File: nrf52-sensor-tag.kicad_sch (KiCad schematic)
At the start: 20 parts, among them IC1 LTR-308ALS-01, IC3 MS860702BA01-50, J3 Conn_01x07_Male, SW1 EVQ-PUA02K, SW2 EVQ-PUA02K, U1 MS88SF2

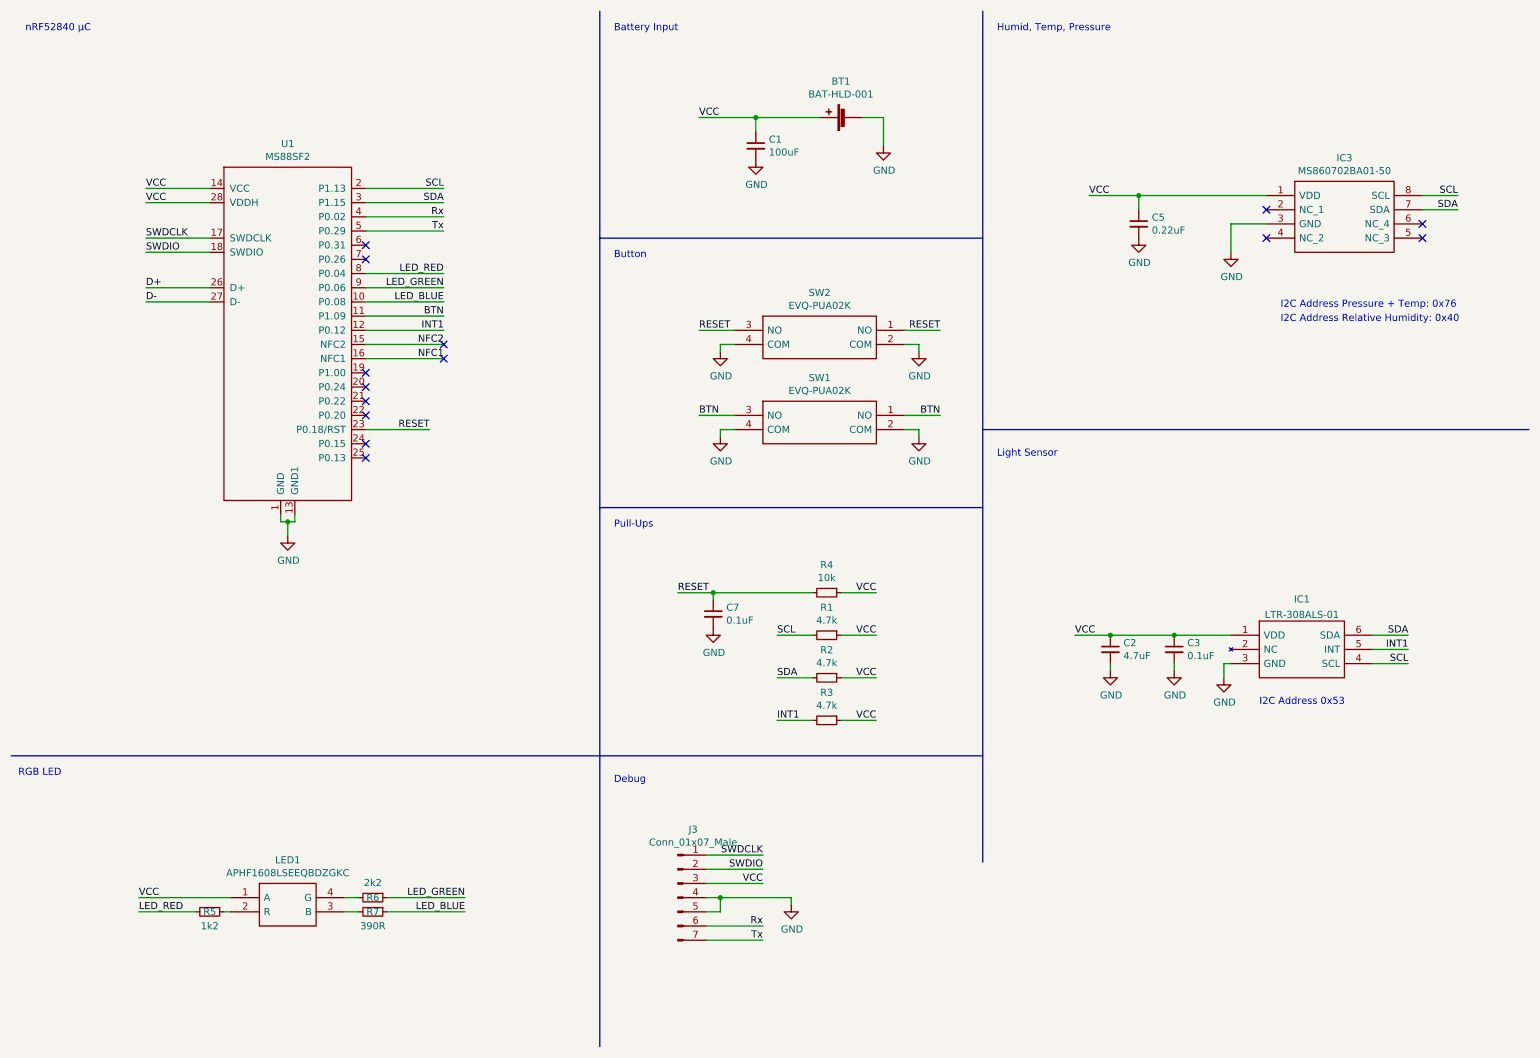
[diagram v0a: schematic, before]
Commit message: Try to fix KiCad Version issue
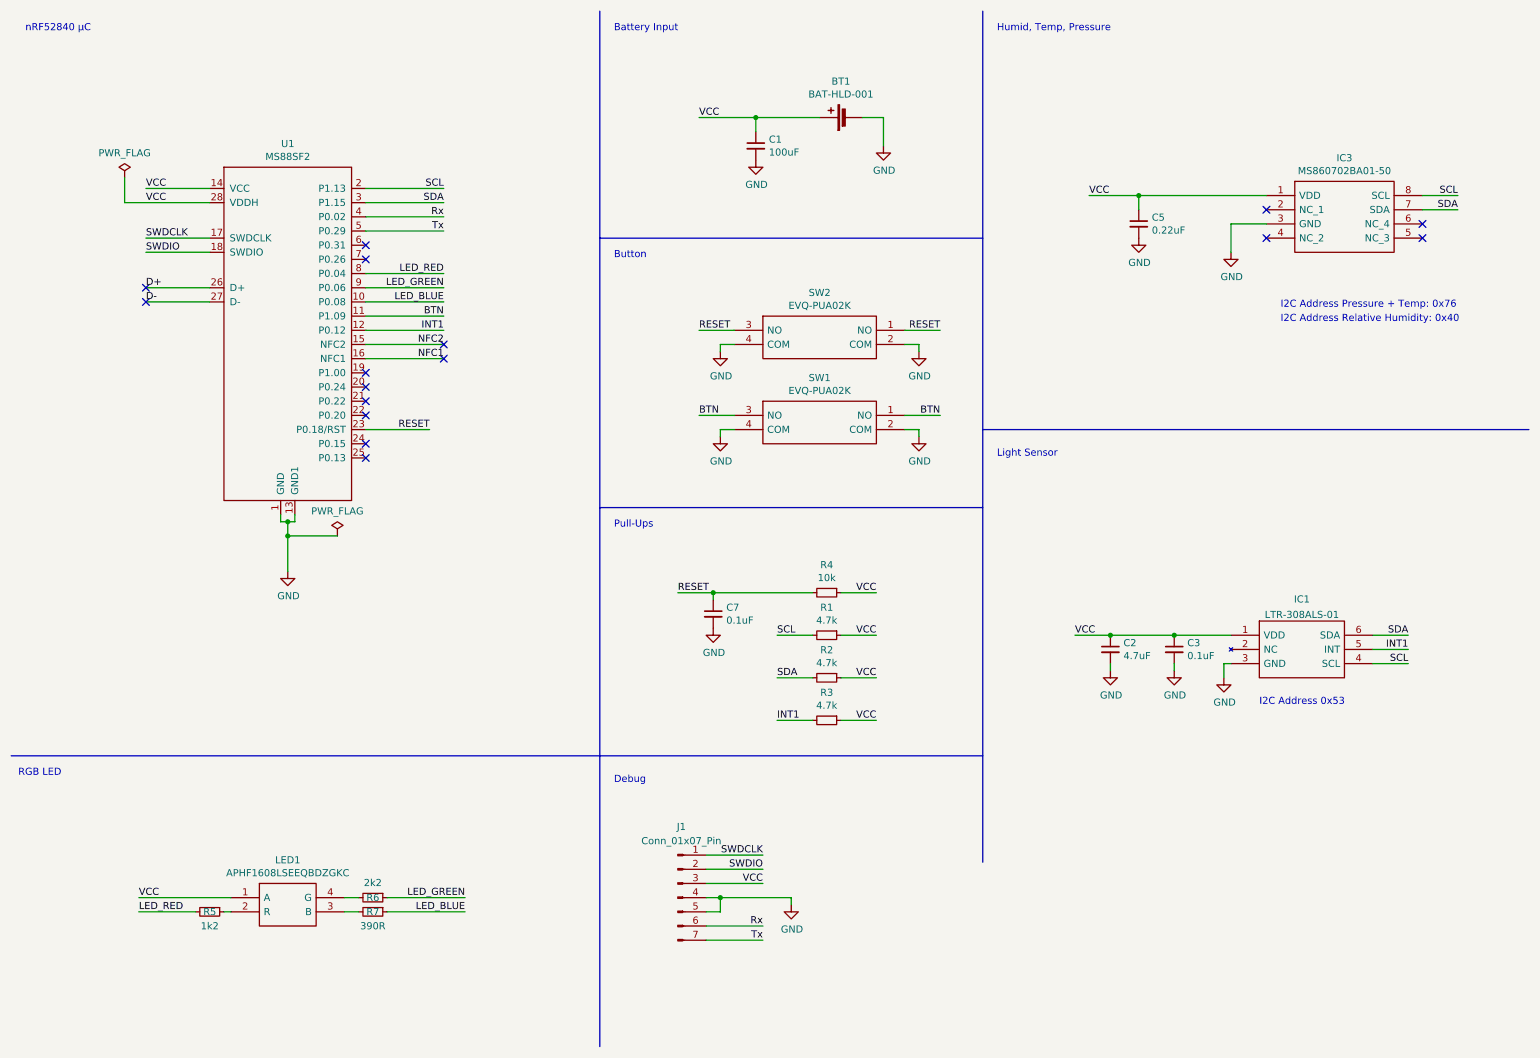
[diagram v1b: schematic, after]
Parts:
- removed J3: Conn_01x07_Male, Connector_PinHeader_2.54mm:PinHeader_1x07_P2.54mm_Vertical, symbol Connector:Conn_01x07_Male
- added J1: Conn_01x07_Pin, Connector_PinSocket_2.54mm:PinSocket_1x07_P2.54mm_Vertical, symbol Connector:Conn_01x07_Pin
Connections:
- net GND: now also J1.4 (Pin_4), J1.5 (Pin_5)
- net Rx: now also J1.6 (Pin_6)
- net SWDCLK: now also J1.1 (Pin_1)
- net SWDIO: now also J1.2 (Pin_2)
- net Tx: now also J1.7 (Pin_7)
- net VCC: now also J1.3 (Pin_3)
- no-connect marks 14 -> 16
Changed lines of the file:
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@@
   (junction (at 139.7 171.45) (diameter 0) (color 0 0 0 0)
   )
+  (junction (at 62.23 104.14) (diameter 0) (color 0 0 0 0)
+  )
   (junction (at 214.63 45.72) (diameter 0) (color 0 0 0 0)
   )
@@
   (junction (at 209.55 124.46) (diameter 0) (color 0 0 0 0)
   )
-  (junction (at 62.23 104.14) (diameter 0) (color 0 0 0 0)
+  (junction (at 62.23 106.68) (diameter 0) (color 0 0 0 0)
   )
   (junction (at 138.43 116.84) (diameter 0) (color 0 0 0 0)
@@
   (no_connect (at 237.49 48.26))
   (no_connect (at 237.49 53.34))
+  (no_connect (at 36.83 62.23))
   (no_connect (at 76.2 90.17))
   (no_connect (at 76.2 57.15))
@@
   (no_connect (at 265.43 53.34))
   (no_connect (at 265.43 50.8))
+  (no_connect (at 36.83 64.77))
   (no_connect (at 90.17 72.39))
   (no_connect (at 76.2 92.71))
@@
     (stroke (width 0) (type default))
   )
+  (wire (pts (xy 33.02 46.99) (xy 33.02 42.545))
+    (stroke (width 0) (type default))
+  )
   (wire (pts (xy 80.01 173.99) (xy 93.98 173.99))
     (stroke (width 0) (type default))
@@
     (stroke (width 0) (type default))
   )
+  (wire (pts (xy 62.23 104.14) (xy 63.5 104.14))
+    (stroke (width 0) (type default))
+  )
   (wire (pts (xy 265.43 48.26) (xy 271.78 48.26))
     (stroke (width 0) (type default))
@@
     (stroke (width 0) (type default))
   )
+  (wire (pts (xy 71.12 106.68) (xy 62.23 106.68))
+    (stroke (width 0) (type default))
+  )
   (wire (pts (xy 90.17 62.23) (xy 76.2 62.23))
     (stroke (width 0) (type default))
@@
     (stroke (width 0) (type default))
   )
-  (wire (pts (xy 62.23 104.14) (xy 63.5 104.14))
+  (wire (pts (xy 60.96 104.14) (xy 62.23 104.14))
+    (stroke (width 0) (type default))
+  )
+  (wire (pts (xy 62.23 106.68) (xy 62.23 104.14))
     (stroke (width 0) (type default))
   )
@@
     (stroke (width 0) (type default))
   )
+  (wire (pts (xy 36.83 64.77) (xy 48.26 64.77))
+    (stroke (width 0) (type default))
+  )
   (wire (pts (xy 231.14 50.8) (xy 231.14 55.88))
     (stroke (width 0) (type default))
   )
-  (wire (pts (xy 36.83 64.77) (xy 48.26 64.77))
-    (stroke (width 0) (type default))
-  )
   (wire (pts (xy 209.55 130.81) (xy 209.55 129.54))
     (stroke (width 0) (type default))
@@
     (stroke (width 0) (type default))
   )
-  (wire (pts (xy 62.23 104.14) (xy 62.23 106.68))
+  (wire (pts (xy 62.23 106.68) (xy 62.23 113.03))
     (stroke (width 0) (type default))
   )
@@
     (stroke (width 0) (type default))
   )
-  (wire (pts (xy 48.26 46.99) (xy 36.83 46.99))
+  (wire (pts (xy 33.02 46.99) (xy 48.26 46.99))
     (stroke (width 0) (type default))
   )
@@
     (stroke (width 0) (type default))
   )
-  (wire (pts (xy 60.96 104.14) (xy 62.23 104.14))
-    (stroke (width 0) (type default))
-  )
   (wire (pts (xy 137.16 171.45) (xy 139.7 171.45))
     (stroke (width 0) (type default))
@@
     (stroke (width 0) (type default))
   )
+  (wire (pts (xy 220.98 130.81) (xy 220.98 129.54))
+    (stroke (width 0) (type default))
+  )
+  (wire (pts (xy 76.2 64.77) (xy 90.17 64.77))
+    (stroke (width 0) (type default))
+  )
+  (wire (pts (xy 220.98 124.46) (xy 231.14 124.46))
+    (stroke (width 0) (type default))
+  )
+  (wire (pts (xy 205.74 45.72) (xy 214.63 45.72))
+    (stroke (width 0) (type default))
+  )
+  (wire (pts (xy 76.2 72.39) (xy 90.17 72.39))
+    (stroke (width 0) (type default))
+  )
+  (wire (pts (xy 72.39 171.45) (xy 74.93 171.45))
+    (stroke (width 0) (type default))
+  )
   (wire (pts (xy 36.83 62.23) (xy 48.26 62.23))
     (stroke (width 0) (type default))
   )
-  (wire (pts (xy 220.98 130.81) (xy 220.98 129.54))
-    (stroke (width 0) (type default))
-  )
-  (wire (pts (xy 76.2 64.77) (xy 90.17 64.77))
-    (stroke (width 0) (type default))
-  )
-  (wire (pts (xy 220.98 124.46) (xy 231.14 124.46))
-    (stroke (width 0) (type default))
-  )
-  (wire (pts (xy 205.74 45.72) (xy 214.63 45.72))
-    (stroke (width 0) (type default))
-  )
-  (wire (pts (xy 76.2 72.39) (xy 90.17 72.39))
-    (stroke (width 0) (type default))
-  )
-  (wire (pts (xy 72.39 171.45) (xy 74.93 171.45))
-    (stroke (width 0) (type default))
-  )
   (wire (pts (xy 138.43 118.11) (xy 138.43 116.84))
     (stroke (width 0) (type default))
@@
         (path "/b3609262-269b-4fe2-a202-5a86fde3ac12"
           (reference "#PWR0118") (unit 1)
-        )
-      )
-    )
-  )
-  (symbol (lib_id "Connector:Conn_01x07_Male") (at 132.08 171.45 0) (unit 1)
-    (in_bom yes) (on_board yes) (dnp no)
-    (property "Reference" "J3" (at 134.8232 159.2326 0)
-      (effects (font (size 1.27 1.27)))
-    )
-    (property "Value" "Conn_01x07_Male" (at 134.8232 161.544 0)
-      (effects (font (size 1.27 1.27)))
-    )
-    (property "Footprint" "Connector_PinHeader_2.54mm:PinHeader_1x07_P2.54mm_Vertical" (at 132.08 171.45 0)
-      (effects (font (size 1.27 1.27)) hide)
-    )
-    (property "Datasheet" "~" (at 132.08 171.45 0)
-      (effects (font (size 1.27 1.27)) hide)
-    )
-    (pin "1")
-    (pin "2")
-    (pin "3")
-    (pin "4")
-    (pin "5")
-    (pin "6")
-    (pin "7")
-    (instances
-      (project "nrf52-sensor-tag"
-        (path "/b3609262-269b-4fe2-a202-5a86fde3ac12"
-          (reference "J3") (unit 1)
         )
       )
@@
     )
   )
-  (symbol (lib_id "power:GND") (at 62.23 106.68 0) (unit 1)
-    (in_bom yes) (on_board yes) (dnp no)
-    (property "Reference" "#PWR0101" (at 62.23 113.03 0)
-      (effects (font (size 1.27 1.27)) hide)
-    )
-    (property "Value" "GND" (at 62.357 111.0742 0)
-      (effects (font (size 1.27 1.27)))
-    )
-    (property "Footprint" "" (at 62.23 106.68 0)
-      (effects (font (size 1.27 1.27)) hide)
-    )
-    (property "Datasheet" "" (at 62.23 106.68 0)
+  (symbol (lib_id "power:GND") (at 62.23 113.03 0) (unit 1)
+    (in_bom yes) (on_board yes) (dnp no)
+    (property "Reference" "#PWR0101" (at 62.23 119.38 0)
+      (effects (font (size 1.27 1.27)) hide)
+    )
+    (property "Value" "GND" (at 62.357 117.4242 0)
+      (effects (font (size 1.27 1.27)))
+    )
+    (property "Footprint" "" (at 62.23 113.03 0)
+      (effects (font (size 1.27 1.27)) hide)
+    )
+    (property "Datasheet" "" (at 62.23 113.03 0)
       (effects (font (size 1.27 1.27)) hide)
     )
@@
         )
       )
+    )
+  )
+  (symbol (lib_id "power:PWR_FLAG") (at 71.12 106.68 0) (unit 1)
+    (in_bom yes) (on_board yes) (dnp no) (fields_autoplaced)
+    (property "Reference" "#FLG02" (at 71.12 104.775 0)
+      (effects (font (size 1.27 1.27)) hide)
+    )
+    (property "Value" "PWR_FLAG" (at 71.12 102.235 0)
+      (effects (font (size 1.27 1.27)))
+    )
+    (property "Footprint" "" (at 71.12 106.68 0)
+      (effects (font (size 1.27 1.27)) hide)
+    )
+    (property "Datasheet" "~" (at 71.12 106.68 0)
+      (effects (font (size 1.27 1.27)) hide)
+    )
+    (pin "1")
+    (instances
+      (project "nrf52-sensor-tag"
+        (path "/b3609262-269b-4fe2-a202-5a86fde3ac12"
+          (reference "#FLG02") (unit 1)
+        )
+      )
+    )
+  )
+  (symbol (lib_id "Connector:Conn_01x07_Pin") (at 132.08 171.45 0) (unit 1)
+    (in_bom no) (on_board yes) (dnp no) (fields_autoplaced)
+    (property "Reference" "J1" (at 132.715 158.75 0)
+      (effects (font (size 1.27 1.27)))
+    )
+    (property "Value" "Conn_01x07_Pin" (at 132.715 161.29 0)
+      (effects (font (size 1.27 1.27)))
+    )
+    (property "Footprint" "Connector_PinSocket_2.54mm:PinSocket_1x07_P2.54mm_Vertical" (at 132.08 171.45 0)
+      (effects (font (size 1.27 1.27)) hide)
+    )
+    (property "Datasheet" "~" (at 132.08 171.45 0)
+      (effects (font (size 1.27 1.27)) hide)
+    )
+    (pin "1")
+    (pin "2")
+    (pin "3")
+    (pin "4")
+    (pin "5")
+    (pin "6")
+    (pin "7")
+    (instances
+      (project "nrf52-sensor-tag"
+        (path "/b3609262-269b-4fe2-a202-5a86fde3ac12"
+          (reference "J1") (unit 1)
+        )
+      )
+    )
+  )
+  (symbol (lib_id "power:PWR_FLAG") (at 33.02 42.545 0) (unit 1)
+    (in_bom yes) (on_board yes) (dnp no) (fields_autoplaced)
+    (property "Reference" "#FLG01" (at 33.02 40.64 0)
+      (effects (font (size 1.27 1.27)) hide)
+    )
+    (property "Value" "PWR_FLAG" (at 33.02 38.1 0)
+      (effects (font (size 1.27 1.27)))
+    )
+    (property "Footprint" "" (at 33.02 42.545 0)
+      (effects (font (size 1.27 1.27)) hide)
+    )
+    (property "Datasheet" "~" (at 33.02 42.545 0)
+      (effects (font (size 1.27 1.27)) hide)
+    )
+    (pin "1")
+    (instances
+      (project "nrf52-sensor-tag"
+        (path "/b3609262-269b-4fe2-a202-5a86fde3ac12"
+          (reference "#FLG01") (unit 1)
+        )
+      )
